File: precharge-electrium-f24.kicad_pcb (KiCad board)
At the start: 2 copper layers, 14 parts, among them J1 ASMPR45-1X2-RK, J2 ASMPR45-1X2-RK, J3 B5B-PH-K-S, Q1 IRFS7530, Q2 IRFS7530, Q3 IRFS7530

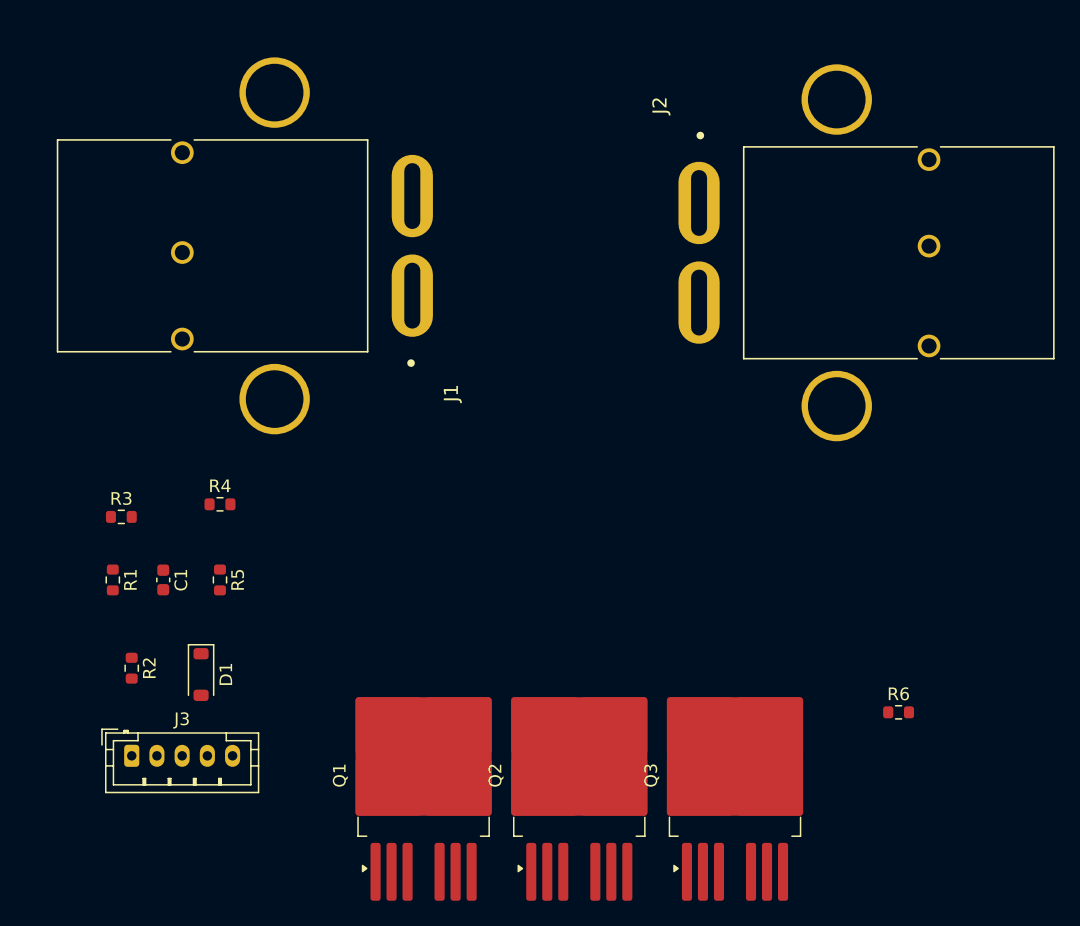
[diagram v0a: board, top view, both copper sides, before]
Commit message: Update PCB layout and fix rules violations
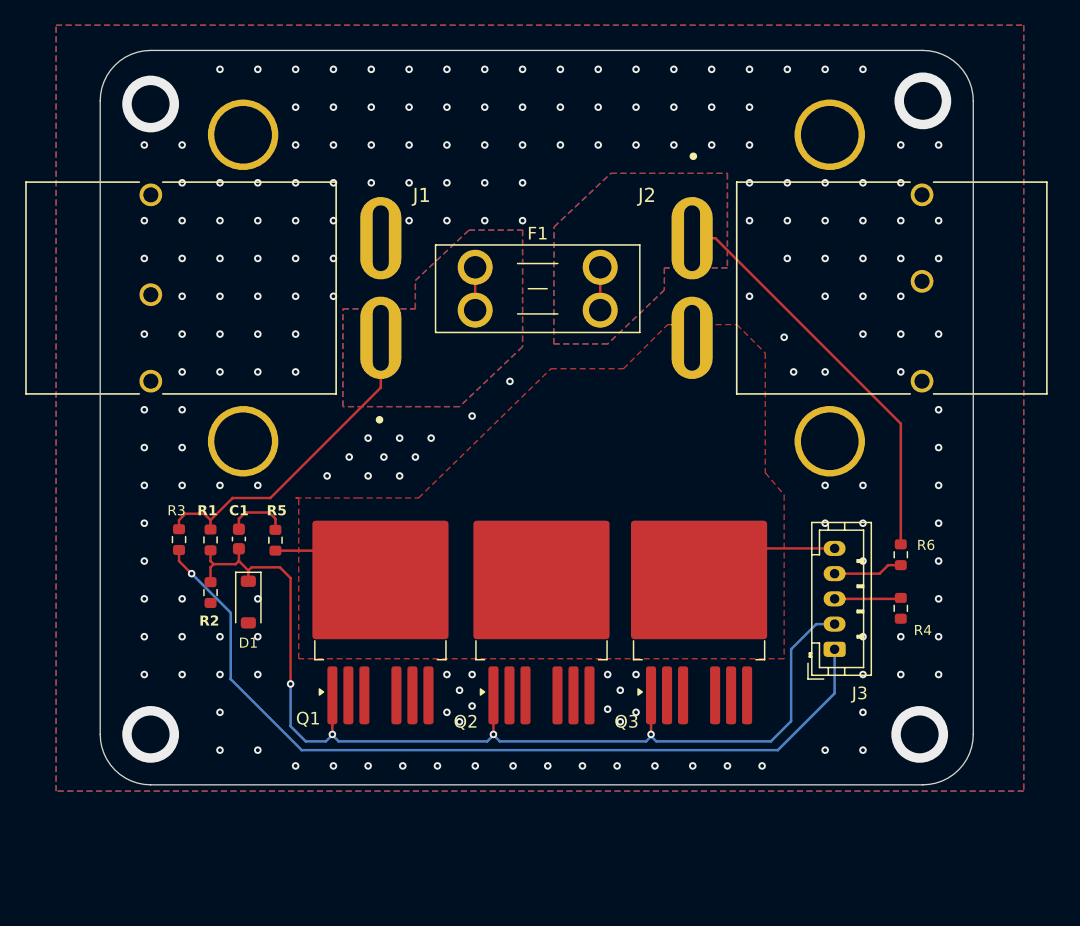
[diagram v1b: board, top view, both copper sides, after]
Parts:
- added F1: 3568, Fuse:Fuseholder_Blade_Mini_Keystone_3568, F.Cu at (144.7, 104.2)
- C1: value 1u, 0603, 60V, X7R -> 1uF, 0603, 60V, X7R
- Q1, Q2, Q3: footprint Package_TO_SOT_SMD:TO-263-6 -> transistor:Package_TO_SOT_SMDTO-263-6-CUSTOM
- R6: value RLED, 0603 -> 10k
- moved J3 56.4 mm to (173.2, 134.5), turned to 90 degrees
- moved R4 54.6 mm to (178.5, 131.2), turned to -90 degrees
- moved Q1 14.4 mm to (137.2, 130.5)
- moved Q2 14.3 mm to (150.0, 130.5)
- moved Q3 14.3 mm to (162.5, 130.5)
- moved R6 12.5 mm to (178.5, 127.0), turned to -90 degrees
- moved R2 8.66 mm to (123.8, 130.0)
- moved R1 8.38 mm to (123.8, 125.8)
- moved D1 6.86 mm to (126.8, 130.8)
- moved C1 6.82 mm to (126.0, 125.8)
- moved R5 5.41 mm to (128.9, 125.8)
- moved R3 4.92 mm to (121.2, 125.8), turned to -90 degrees
- moved J1 4.18 mm to (137.3, 109.8)
- moved J2 2.85 mm to (161.9, 101.9)
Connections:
- D1 pad 2: -BATT -> GND
- J1 pad 1: -BATT -> VCC
- J1 pad 2: +BATT -> GND
- J2 pad 1: -VOUT -> OUT+
- J2 pad 2: +BATT -> OUT-
- J3 pad 5: -VOUT -> OUT-
- Q1 pad 2: -BATT -> GND
- Q1 pad 3: -BATT -> GND
- Q1 pad 4: -VOUT -> OUT-
- Q1 pad 5: -BATT -> GND
- Q1 pad 6: -BATT -> GND
- Q1 pad 7: -BATT -> GND
- Q2 pad 2: -BATT -> GND
- Q2 pad 3: -BATT -> GND
- Q2 pad 4: -VOUT -> OUT-
- Q2 pad 5: -BATT -> GND
- Q2 pad 6: -BATT -> GND
- Q2 pad 7: -BATT -> GND
- Q3 pad 2: -BATT -> GND
- Q3 pad 3: -BATT -> GND
- Q3 pad 4: -VOUT -> OUT-
- Q3 pad 5: -BATT -> GND
- Q3 pad 6: -BATT -> GND
- Q3 pad 7: -BATT -> GND
- R1 pad 1: +BATT -> VCC
- R2 pad 2: -BATT -> GND
- R3 pad 1: +BATT -> VCC
- R4 pad 2: -BATT -> GND
- R5 pad 2: -VOUT -> OUT-
- R6 pad 1: +BATT -> OUT+
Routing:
- net /SW: track 0.00 -> 85.0 mm, vias 0 -> 4
- net /NO: track 0.00 -> 67.5 mm, vias 0 -> 1
- net OUT+: track 0.00 -> 36.0 mm
- net VCC: track 0.00 -> 29.6 mm
- net OUT-: track 0.00 -> 13.6 mm
- net /+LED: track 0.00 -> 5.53 mm
- net /NC: track 0.00 -> 5.28 mm
- net Net-(C1-Pad1): track 0.00 -> 5.01 mm
- net GND: vias 0 -> 196
- net (no net): vias 0 -> 4
- added copper zone on B.Cu, net GND
- added copper zone on F.Cu, net GND
- added copper zone on B.Cu, net OUT+
- added copper zone on F.Cu, net OUT+
- added copper zone on F.Cu, net OUT-
- added copper zone on B.Cu, net VCC
- added copper zone on F.Cu, net VCC
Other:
- board outline added: 69.2 x 58.2 mm
- board text added: "{ "ViaStitching": "0.2", "stitch_zone_0": { "HSpacing": "1", "VSpacing": "1", "HOffset": "0", "VOffset": "0", "Clearance": "0", "Randomize": false }, "stitch_zone_1": { "HSpacing": "3", "VSpacing": "3", "HOffset": "1", "VOffset": "0.5", "Clearance": "0.3", "Randomize": false } }"
